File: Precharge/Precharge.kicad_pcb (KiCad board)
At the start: 2 copper layers, 63.5 x 53.3 mm, 10 parts, among them J1 1053091202, J2 1053091203, J3 1053091202, K1 Relay_SPST-NO, K2 Relay_SPST-NO

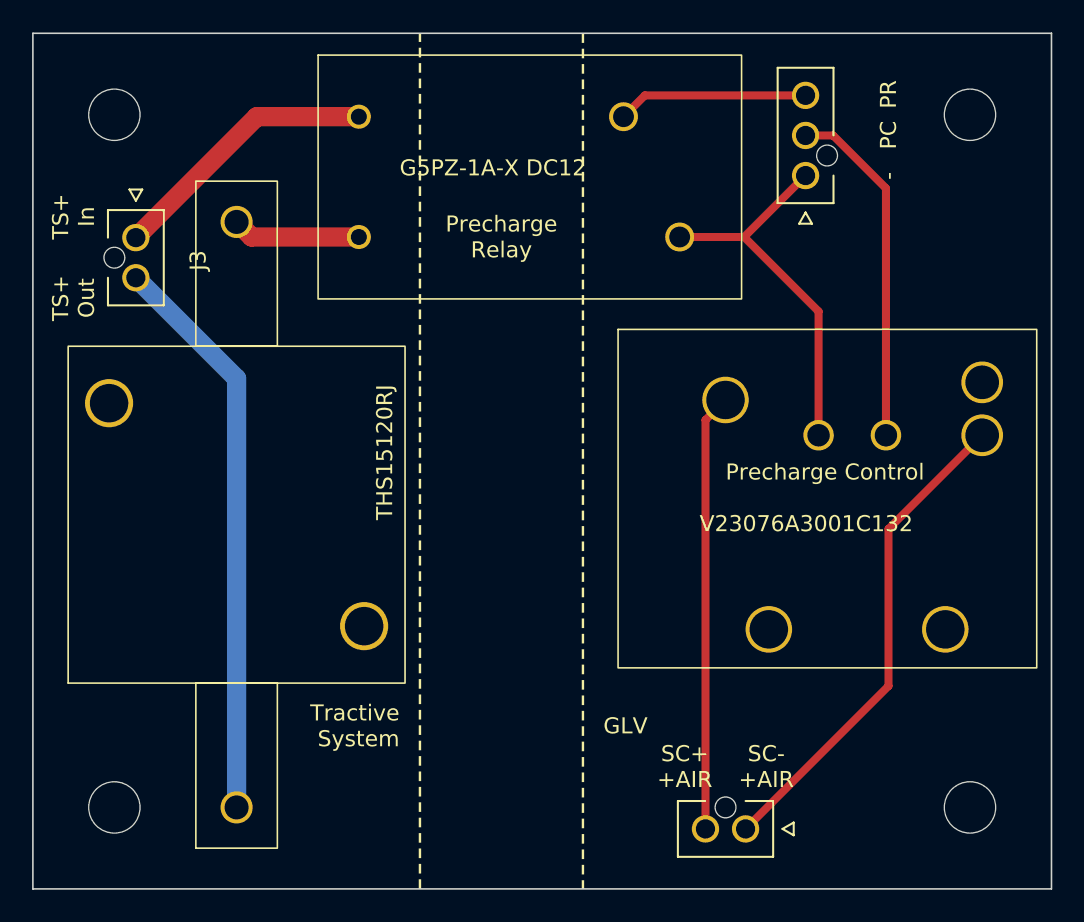
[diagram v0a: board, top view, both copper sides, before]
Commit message: Added diodes to Precharge PCB
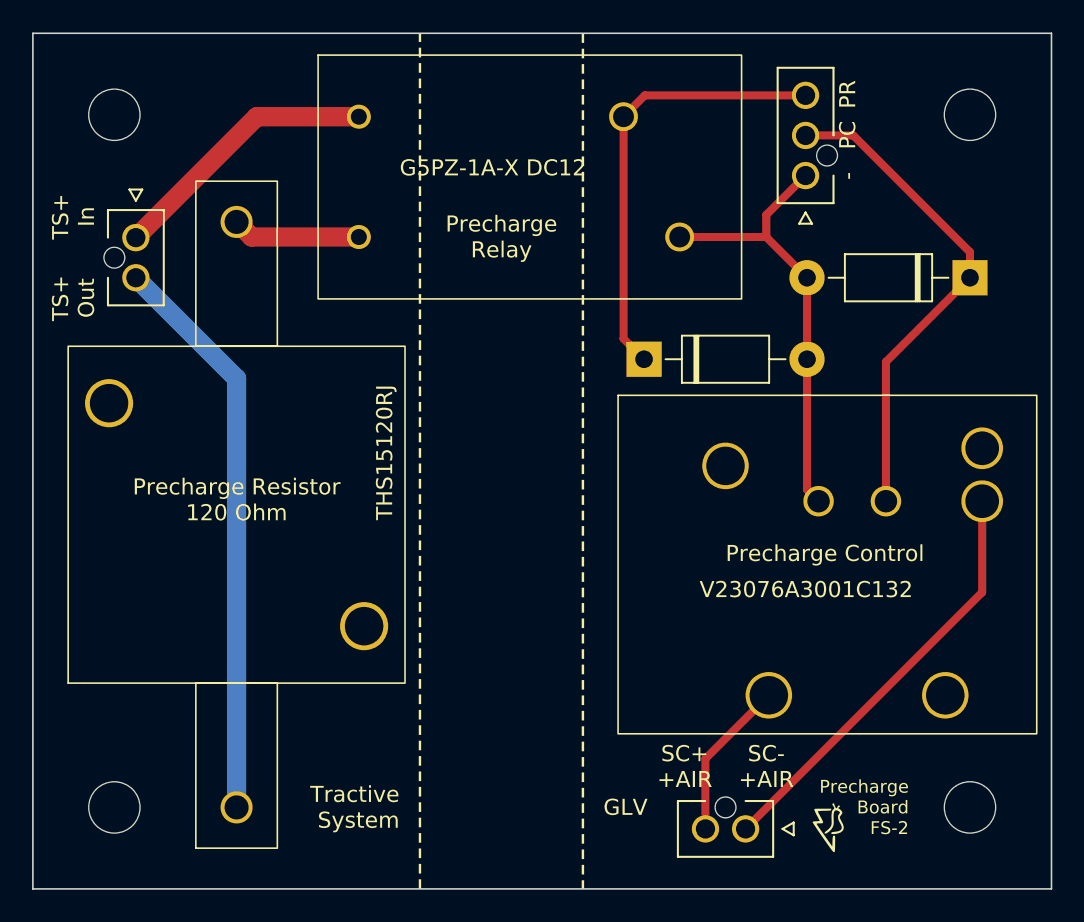
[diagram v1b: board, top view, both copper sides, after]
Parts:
- added D3: 1N4001, Diode_THT:D_DO-41_SOD81_P10.16mm_Horizontal, F.Cu at (71.1, 27.9)
- added D4: 1N4001, Diode_THT:D_DO-41_SOD81_P10.16mm_Horizontal, F.Cu at (50.8, 33.0)
- added G***: LOGO, Precharge_Library:FORMULA SLUG, F.Cu at (65.4, 62.3)
- moved K2 4.11 mm to (49.2, 35.3)
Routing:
- net /SC_+AIR_+: track 27.4 -> 9.97 mm
- net /Precharge_Relay: track 11.9 -> 27.6 mm
- net /Precharge_Control: track 21.8 -> 31.1 mm
- net /GLV-: track 23.7 -> 28.1 mm
- net /SC_+AIR_-: track 30.6 -> 26.5 mm
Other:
- board text added: "Precharge Board FS-2"
- board text added: "Precharge Resistor 120 Ohm"
